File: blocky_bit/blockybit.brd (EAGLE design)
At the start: 51.4 x 50.1 mm, 99 parts, among them IC2 PAM8301, IC4 LIS3DH, U1 ESP-WROOM-32, U2 AP2112-3.3, U3 ATMEGA32U4, X1 JSTPH, Y2 16MHz

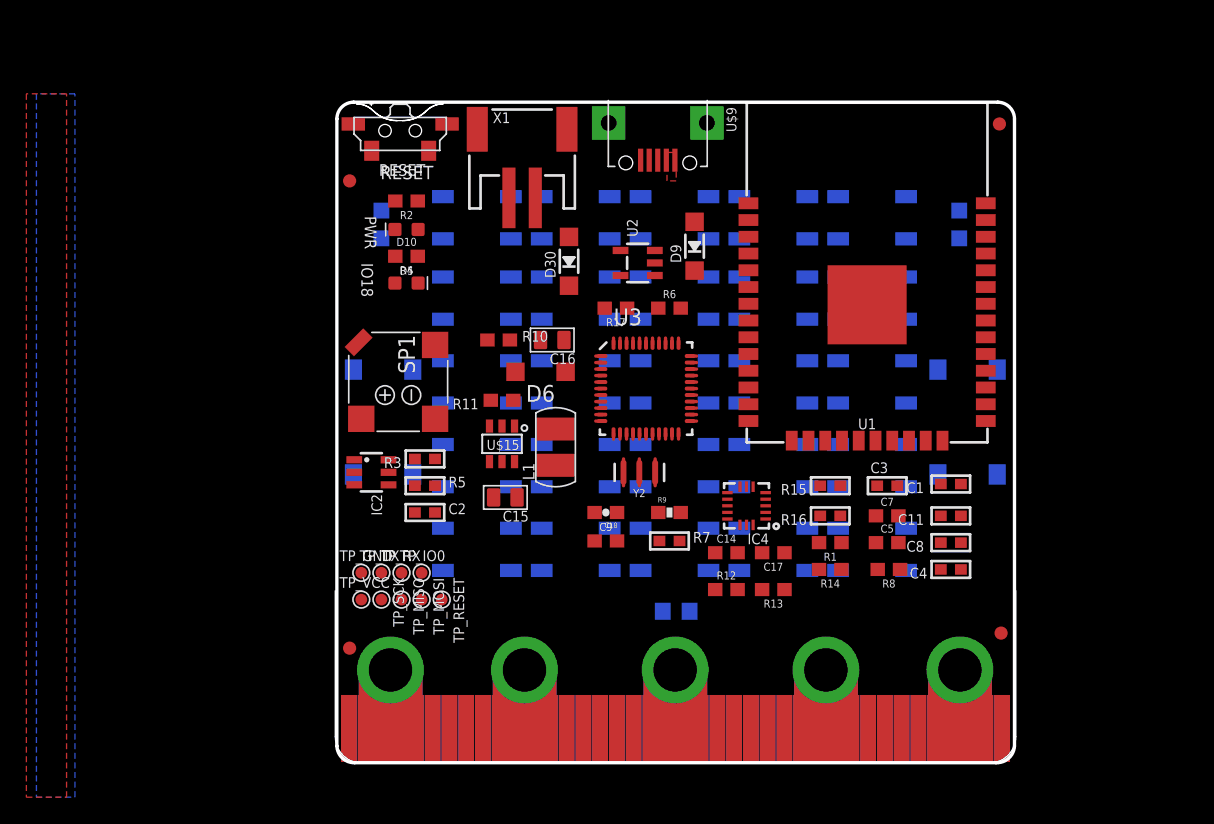
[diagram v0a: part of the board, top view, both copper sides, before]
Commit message: Update new layout for blockybit
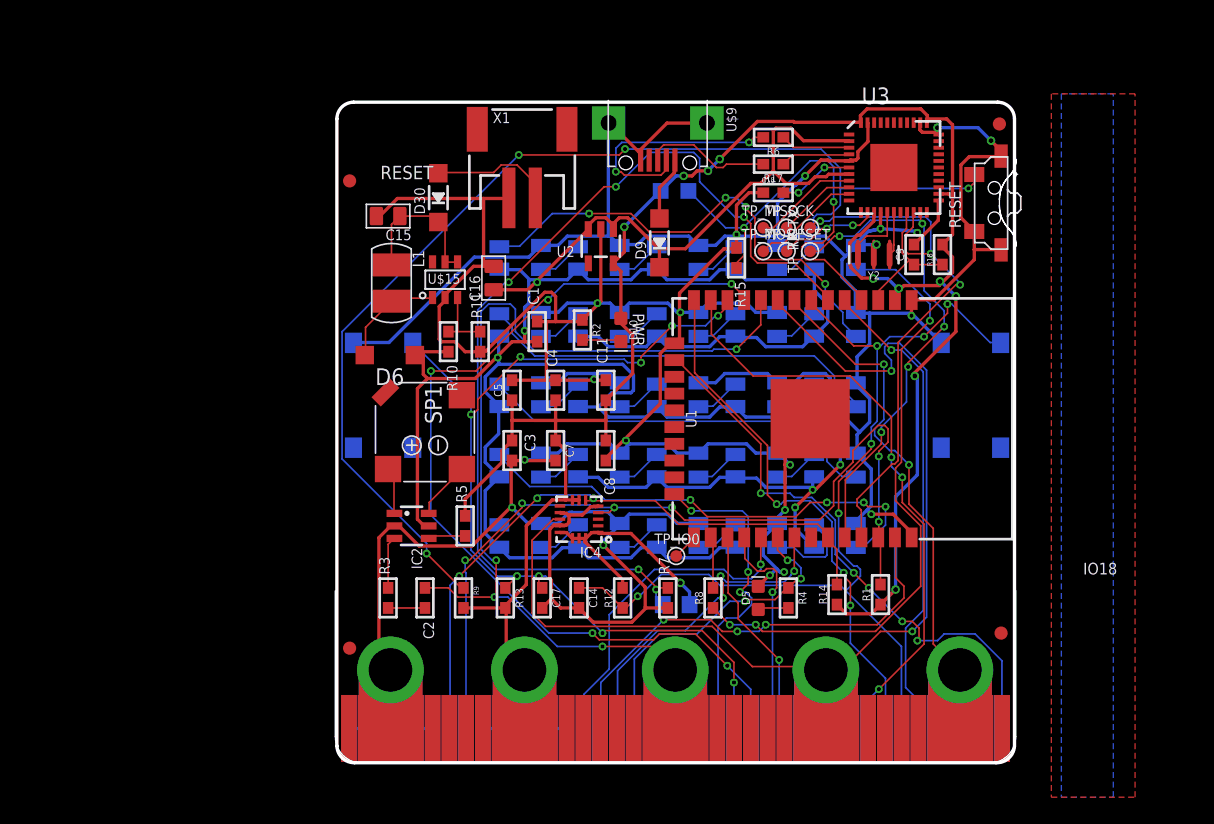
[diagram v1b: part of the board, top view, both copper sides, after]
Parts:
- removed LEFT_LIGHT_SENSOR, RIGHT_LIGHT_SENSOR: (no value), microbuilder:CHIPLED_0805
- removed R16: 11K, microbuilder:_0603
- removed TP_GND, TP_VCC: (no value), Discrete:TP_3535
- removed U$4: (no value), Anata-Symbols:BLOCKY_LOGO
- added LIGHT_SENSOR: (no value), microbuilder:CHIPLED_0805
- added R18: 10K, microbuilder:_0603
- C14, C17, C5, C7, C9: device SparkFun-Capacitors:0603 -> microbuilder:_0603
- C18: device SparkFun:0603-CAP -> microbuilder:_0603
- R1, R10, R11, R12, R13, R14, R17, R2, R4, R6, R8: device SparkFun-Resistors:0603 -> microbuilder:_0603
- R9: device SparkFun:0603-RES -> microbuilder:_0603
- RGB1, RGB10, RGB11, RGB12, RGB13, RGB14, RGB15, RGB16, RGB17, RGB18, RGB19, RGB2, RGB20, RGB21, RGB22, RGB23, RGB24, RGB25, RGB3, RGB4, RGB5, RGB6, RGB7, RGB8, RGB9: device SparkFun-LED:WS2812B -> Blocky:WS2812B-3535
- U3: value ATMEGA32U4 -> 32U4; device Testing:QFN-44-NOPAD_1:1-OUTFAKES -> SparkFun-IC-Microcontroller:QFN-44
- moved RESET 45.4 mm to (52.8, 45.1), turned to 90 degrees
- moved TP_TX 41.7 mm to (38.9, 43.2), turned to 90 degrees
- moved TP_SCK 41.7 mm to (37.1, 43.2), turned to 0 degrees
- moved TP_RX 39.4 mm to (38.9, 41.4), turned to 90 degrees
- moved TP_MISO 39.3 mm to (35.3, 43.2), turned to 0 degrees
- moved R4 38.9 mm to (37.2, 15.1), turned to 270 degrees
- moved TP_RESET 37.2 mm to (37.1, 41.4), turned to 0 degrees
- moved TP_MOSI 37.0 mm to (35.3, 41.4), turned to 0 degrees
- moved D5 35.8 mm to (34.9, 15.1), turned to 90 degrees
- moved C1 33.4 mm to (18.2, 35.3), turned to 90 degrees
- moved C4 32.9 mm to (19.6, 30.9), turned to 90 degrees
- moved C9 31.9 mm to (46.7, 41.1), turned to 90 degrees
- moved C5 30.7 mm to (16.3, 30.9), turned to 90 degrees
- moved C3 28.6 mm to (16.3, 26.3), turned to 270 degrees
- moved C11 27.8 mm to (23.4, 30.9), turned to 90 degrees
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- renumbered U$12 to PAD_3V3, U$13 to PAD_GND, U$6 to PAD_IO25, U$7 to PAD_IO33, U$8 to PAD_IO32
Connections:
- net N$30 renamed UCAP
- removed net IO02: U$1.P$18, U$1.P$58
- removed net RESET: C9.1, R9.1, RESET.2, TP_RESET.T, U1.3, U3.13, U3.19
- removed net VCC: R9.2, U3.14, U3.24, U3.34, U3.44
- new net 32U4_RST: R9.1, RESET.2, TP_RESET.T, U3.13
- new net ESP_RST: C9.1, R18.1, U1.3, U3.19
- net 3.3V: now also LIGHT_SENSOR.A, R18.2, R9.2, U3.14, U3.24, U3.34, U3.44; no longer LEFT_LIGHT_SENSOR.A, RIGHT_LIGHT_SENSOR.A, TP_VCC.T, U$1.P$27, U$1.P$28, U$1.P$29, U$1.P$30, U$1.P$31, U$1.P$32
- net GND: now also RGB14.3; no longer R16.1, TP_GND.T, U$1.P$35, U$1.P$36, U$1.P$37, U$1.P$38, U$1.P$39, U$1.P$40
- net IO12: no longer U$1.P$8
- net IO13: no longer U$1.P$1
- net IO14: no longer U$1.P$9
- net IO16: no longer U$1.P$14, U$1.P$46, U$1.P$6
- net IO17: no longer U$1.P$15
- net IO18: no longer U$1.P$23, U3.18
- net IO19: no longer U$1.P$24
- net IO2: now also U$1.P$58
- net IO23: no longer U$1.P$25
- net IO25: now also PAD_IO25.PAD, U$1.P$59, U$1.P$60, U$1.P$61, U$1.P$62; no longer PAD_IO32.PAD, U$1.P$2, U$1.P$3, U$1.P$4, U$1.P$42, U$1.P$43, U$1.P$44, U$1.P$45, U$1.P$5
- net IO26: no longer U$1.P$16
- net IO27: no longer U$1.P$17
- net IO32: now also PAD_IO32.PAD, U$1.P$42, U$1.P$43, U$1.P$44, U$1.P$45; no longer PAD_IO33.PAD, U$1.P$10, U$1.P$11, U$1.P$12, U$1.P$13, U$1.P$50, U$1.P$51, U$1.P$52, U$1.P$53
- net IO33: now also PAD_IO33.PAD, U$1.P$50, U$1.P$51, U$1.P$52, U$1.P$53; no longer PAD_IO25.PAD, U$1.P$19, U$1.P$20, U$1.P$21, U$1.P$22, U$1.P$59, U$1.P$60, U$1.P$61, U$1.P$62
- net IO35: no longer U$1.P$7
- net IO36: now also LIGHT_SENSOR.C; no longer LEFT_LIGHT_SENSOR.C
- net IO39: now also U$1.P$46; no longer R16.2, RIGHT_LIGHT_SENSOR.C
- net IO5: no longer U$1.P$26
- net SCL_22: no longer U$1.P$33
- net SDA_21: no longer U$1.P$34
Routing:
- net GND: track 0.00 -> 410.5 mm, vias 0 -> 20
- net 5V: track 0.00 -> 237.3 mm, vias 0 -> 6
- net 3.3V: track 0.00 -> 183.9 mm, vias 0 -> 11
- net 32U4_RST: track 0.00 -> 92.9 mm, vias 0 -> 6
- net IO33: track 0.00 -> 86.1 mm, vias 0 -> 2
- net IO25: track 0.00 -> 79.1 mm, vias 0 -> 4
- net IO35: track 0.00 -> 74.6 mm, vias 0 -> 6
- net IO34: track 0.00 -> 74.3 mm, vias 0 -> 5
- net IO27: track 0.00 -> 72.8 mm, vias 0 -> 9
- net IO26: track 0.00 -> 71.3 mm, vias 0 -> 5
- net SCL_22: track 0.00 -> 65.6 mm, vias 0 -> 6
- net SDA_21: track 0.00 -> 48.4 mm, vias 0 -> 3
- net N$23: track 0.00 -> 47.9 mm, vias 0 -> 3
- net IO32: track 0.00 -> 45.7 mm, vias 0 -> 2
- net IO14: track 0.00 -> 45.3 mm, vias 0 -> 3
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- removed copper zone on layer 1, net 5V
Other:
- board size 51.4 x 50.1 mm -> 51.6 x 50.1 mm
- board text removed: "Blocky ESP32"
